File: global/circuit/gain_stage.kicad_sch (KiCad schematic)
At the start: 9 parts, among them U3 TL081H

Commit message: distortion rev 3
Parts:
- Gain1: footprint Connector_PinHeader_2.54mm:PinHeader_1x03_P2.54mm_Vertical -> effect_pedal:potentiometer_wired_23_connected
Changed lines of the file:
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@@
       (effects (font (size 1.27 1.27)) hide)
     )
-    (property "Footprint" "Connector_PinHeader_2.54mm:PinHeader_1x03_P2.54mm_Vertical" (id 2) (at 111.76 64.77 0)
+    (property "Footprint" "effect_pedal:potentiometer_wired_23_connected" (id 2) (at 111.76 64.77 0)
       (effects (font (size 1.27 1.27)) hide)
     )

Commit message: rework global circuits
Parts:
- renumbered C6 to C?, C8 to C?, C7 to C?, Gain1 to Gain?, R5 to R?, R2 to R?, R4 to R?, TP6 to TP?, U3 to U?
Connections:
- net effect_out renamed gain_in
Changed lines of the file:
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@@
     )
   )
-  (global_label "effect_out" (shape input) (at 66.04 56.515 180) (fields_autoplaced)
+  (global_label "gain_in" (shape input) (at 66.04 56.515 180) (fields_autoplaced)
     (effects (font (size 1.27 1.27)) (justify right))
-    (property "Intersheet References" "${INTERSHEET_REFS}" (id 0) (at 54.1926 56.4356 0)
+    (property "Intersheet References" "${INTERSHEET_REFS}" (id 0) (at 56.8536 56.4356 0)
       (effects (font (size 1.27 1.27)) (justify right) hide)
     )
@@
   (symbol (lib_id "Device:C") (at 111.125 41.91 0) (unit 1)
     (in_bom yes) (on_board yes)
-    (property "Reference" "C6" (id 0) (at 112.395 40.005 0)
+    (property "Reference" "C?" (id 0) (at 112.395 40.005 0)
       (effects (font (size 1.27 1.27)) (justify left))
     )
@@
   (symbol (lib_id "Device:R") (at 122.555 64.77 270) (unit 1)
     (in_bom yes) (on_board yes)
-    (property "Reference" "R5" (id 0) (at 122.555 69.85 90))
+    (property "Reference" "R?" (id 0) (at 122.555 69.85 90))
     (property "Value" "R" (id 1) (at 122.555 67.31 90)
       (effects (font (size 1.27 1.27)) hide)
@@
   (symbol (lib_id "Device:R_Potentiometer") (at 111.76 64.77 270) (unit 1)
     (in_bom yes) (on_board yes)
-    (property "Reference" "Gain1" (id 0) (at 111.76 69.85 90))
+    (property "Reference" "Gain?" (id 0) (at 111.76 69.85 90))
     (property "Value" "10k" (id 1) (at 111.76 71.12 90)
       (effects (font (size 1.27 1.27)) hide)
@@
   (symbol (lib_id "Amplifier_Operational:TL081H") (at 101.6 53.975 0) (unit 1)
     (in_bom yes) (on_board yes)
-    (property "Reference" "U3" (id 0) (at 106.045 59.055 0))
+    (property "Reference" "U?" (id 0) (at 106.045 59.055 0))
     (property "Value" "TL081H" (id 1) (at 108.585 57.15 0))
     (property "Footprint" "Package_TO_SOT_SMD:SOT-23-5_HandSoldering" (id 2) (at 101.6 53.975 0)
@@
   (symbol (lib_id "Device:R") (at 74.295 56.515 270) (unit 1)
     (in_bom yes) (on_board yes)
-    (property "Reference" "R2" (id 0) (at 74.295 53.975 90))
+    (property "Reference" "R?" (id 0) (at 74.295 53.975 90))
     (property "Value" "R" (id 1) (at 74.295 52.07 90)
       (effects (font (size 1.27 1.27)) hide)
@@
   (symbol (lib_id "power:GND") (at 101.6 73.66 0) (unit 1)
     (in_bom yes) (on_board yes) (fields_autoplaced)
-    (property "Reference" "#PWR0104" (id 0) (at 101.6 80.01 0)
+    (property "Reference" "#PWR?" (id 0) (at 101.6 80.01 0)
       (effects (font (size 1.27 1.27)) hide)
     )
@@
   (symbol (lib_id "Device:C") (at 134.62 53.975 90) (unit 1)
     (in_bom yes) (on_board yes)
-    (property "Reference" "C8" (id 0) (at 134.62 58.42 90))
+    (property "Reference" "C?" (id 0) (at 134.62 58.42 90))
     (property "Value" "C" (id 1) (at 134.62 57.785 90)
       (effects (font (size 1.27 1.27)) hide)
@@
   (symbol (lib_id "power:GND") (at 111.125 45.72 0) (unit 1)
     (in_bom yes) (on_board yes)
-    (property "Reference" "#PWR0102" (id 0) (at 111.125 52.07 0)
+    (property "Reference" "#PWR?" (id 0) (at 111.125 52.07 0)
       (effects (font (size 1.27 1.27)) hide)
     )
@@
   (symbol (lib_id "power:+4V") (at 84.455 73.66 180) (unit 1)
     (in_bom yes) (on_board yes) (fields_autoplaced)
-    (property "Reference" "#PWR0115" (id 0) (at 84.455 69.85 0)
+    (property "Reference" "#PWR?" (id 0) (at 84.455 69.85 0)
       (effects (font (size 1.27 1.27)) hide)
     )
@@
   (symbol (lib_id "power:+8V") (at 101.6 37.465 0) (unit 1)
     (in_bom yes) (on_board yes)
-    (property "Reference" "#PWR024" (id 0) (at 101.6 41.275 0)
+    (property "Reference" "#PWR?" (id 0) (at 101.6 41.275 0)
       (effects (font (size 1.27 1.27)) hide)
     )
@@
   (symbol (lib_id "Connector:TestPoint") (at 128.905 53.975 0) (unit 1)
     (in_bom yes) (on_board yes)
-    (property "Reference" "TP6" (id 0) (at 127 48.26 0)
+    (property "Reference" "TP?" (id 0) (at 127 48.26 0)
       (effects (font (size 1.27 1.27)) (justify left))
     )
@@
   (symbol (lib_id "Device:R") (at 84.455 65.405 0) (unit 1)
     (in_bom yes) (on_board yes)
-    (property "Reference" "R4" (id 0) (at 86.36 65.405 0)
+    (property "Reference" "R?" (id 0) (at 86.36 65.405 0)
       (effects (font (size 1.27 1.27)) (justify left))
     )
@@
   (symbol (lib_id "Device:C") (at 120.65 41.91 0) (unit 1)
     (in_bom yes) (on_board yes)
-    (property "Reference" "C7" (id 0) (at 121.92 40.005 0)
+    (property "Reference" "C?" (id 0) (at 121.92 40.005 0)
       (effects (font (size 1.27 1.27)) (justify left))
     )
@@
   (symbol (lib_id "power:GND") (at 120.65 45.72 0) (unit 1)
     (in_bom yes) (on_board yes)
-    (property "Reference" "#PWR0103" (id 0) (at 120.65 52.07 0)
-      (effects (font (size 1.27 1.27)) hide)
-    )
+    (property "Reference" "#PWR?" (id 0) (at 120.65 52.07 0)
+      (effects (font (size 1.27 1.27)) hide)
+    )

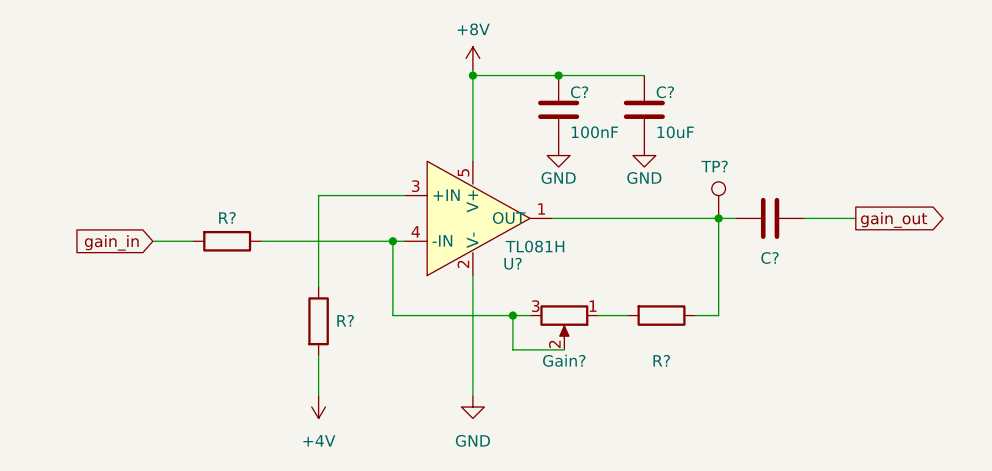
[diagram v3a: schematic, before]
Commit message: minor circuit rework for better use with multiple projects
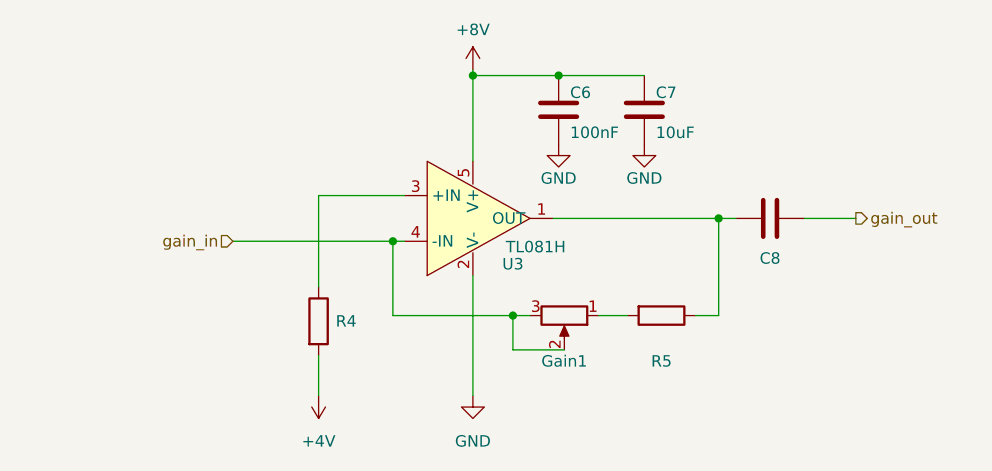
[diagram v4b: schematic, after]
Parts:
- removed R?: R, Resistor_SMD:R_0805_2012Metric_Pad1.20x1.40mm_HandSolder, symbol Device:R
- removed TP?: TestPoint, TestPoint:TestPoint_THTPad_1.0x1.0mm_Drill0.5mm, symbol Connector:TestPoint
- gave numbers to parts that had none: 7
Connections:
- net gain_in: now also Gain1.2, Gain1.3, U3.4 (-IN)
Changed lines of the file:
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@@
-    (stroke (width 0) (type default) (color 0 0 0 0))
-  )
-  (wire (pts (xy 66.04 56.515) (xy 70.485 56.515))
     (stroke (width 0) (type default) (color 0 0 0 0))
   )
@@
     (stroke (width 0) (type default) (color 0 0 0 0))
   )
-  (wire (pts (xy 78.105 56.515) (xy 92.71 56.515))
+  (wire (pts (xy 74.93 56.515) (xy 92.71 56.515))
     (stroke (width 0) (type default) (color 0 0 0 0))
   )
@@
     (stroke (width 0) (type default) (color 0 0 0 0))
   )
-  (global_label "gain_out" (shape output) (at 144.145 53.975 0) (fields_autoplaced)
+  (hierarchical_label "gain_in" (shape input) (at 74.93 56.515 180)
+    (effects (font (size 1.27 1.27)) (justify right))
+  )
+  (hierarchical_label "gain_out" (shape output) (at 144.145 53.975 0)
     (effects (font (size 1.27 1.27)) (justify left))
-    (property "Intersheet References" "${INTERSHEET_REFS}" (id 0) (at 154.6014 53.8956 0)
-      (effects (font (size 1.27 1.27)) (justify left) hide)
-    )
-  )
-  (global_label "gain_in" (shape input) (at 66.04 56.515 180) (fields_autoplaced)
-    (effects (font (size 1.27 1.27)) (justify right))
-    (property "Intersheet References" "${INTERSHEET_REFS}" (id 0) (at 56.8536 56.4356 0)
-      (effects (font (size 1.27 1.27)) (justify right) hide)
-    )
   )
   (symbol (lib_id "Device:C") (at 111.125 41.91 0) (unit 1)
     (in_bom yes) (on_board yes)
-    (property "Reference" "C?" (id 0) (at 112.395 40.005 0)
+    (property "Reference" "C6" (id 0) (at 112.395 40.005 0)
       (effects (font (size 1.27 1.27)) (justify left))
     )
@@
   (symbol (lib_id "Device:R") (at 122.555 64.77 270) (unit 1)
     (in_bom yes) (on_board yes)
-    (property "Reference" "R?" (id 0) (at 122.555 69.85 90))
+    (property "Reference" "R5" (id 0) (at 122.555 69.85 90))
     (property "Value" "R" (id 1) (at 122.555 67.31 90)
       (effects (font (size 1.27 1.27)) hide)
@@
   (symbol (lib_id "Device:R_Potentiometer") (at 111.76 64.77 270) (unit 1)
     (in_bom yes) (on_board yes)
-    (property "Reference" "Gain?" (id 0) (at 111.76 69.85 90))
+    (property "Reference" "Gain1" (id 0) (at 111.76 69.85 90))
     (property "Value" "10k" (id 1) (at 111.76 71.12 90)
       (effects (font (size 1.27 1.27)) hide)
@@
   (symbol (lib_id "Amplifier_Operational:TL081H") (at 101.6 53.975 0) (unit 1)
     (in_bom yes) (on_board yes)
-    (property "Reference" "U?" (id 0) (at 106.045 59.055 0))
+    (property "Reference" "U3" (id 0) (at 106.045 59.055 0))
     (property "Value" "TL081H" (id 1) (at 108.585 57.15 0))
     (property "Footprint" "Package_TO_SOT_SMD:SOT-23-5_HandSoldering" (id 2) (at 101.6 53.975 0)
@@
     (pin "5")
   )
-  (symbol (lib_id "Device:R") (at 74.295 56.515 270) (unit 1)
-    (in_bom yes) (on_board yes)
-    (property "Reference" "R?" (id 0) (at 74.295 53.975 90))
-    (property "Value" "R" (id 1) (at 74.295 52.07 90)
-      (effects (font (size 1.27 1.27)) hide)
-    )
-    (property "Footprint" "Resistor_SMD:R_0805_2012Metric_Pad1.20x1.40mm_HandSolder" (id 2) (at 74.295 54.737 90)
-      (effects (font (size 1.27 1.27)) hide)
-    )
-    (property "Datasheet" "~" (id 3) (at 74.295 56.515 0)
-      (effects (font (size 1.27 1.27)) hide)
-    )
-    (pin "1")
-    (pin "2")
-  )
   (symbol (lib_id "power:GND") (at 101.6 73.66 0) (unit 1)
     (in_bom yes) (on_board yes) (fields_autoplaced)
-    (property "Reference" "#PWR?" (id 0) (at 101.6 80.01 0)
+    (property "Reference" "#PWR0104" (id 0) (at 101.6 80.01 0)
       (effects (font (size 1.27 1.27)) hide)
     )
@@
   (symbol (lib_id "Device:C") (at 134.62 53.975 90) (unit 1)
     (in_bom yes) (on_board yes)
-    (property "Reference" "C?" (id 0) (at 134.62 58.42 90))
+    (property "Reference" "C8" (id 0) (at 134.62 58.42 90))
     (property "Value" "C" (id 1) (at 134.62 57.785 90)
       (effects (font (size 1.27 1.27)) hide)
@@
   (symbol (lib_id "power:GND") (at 111.125 45.72 0) (unit 1)
     (in_bom yes) (on_board yes)
-    (property "Reference" "#PWR?" (id 0) (at 111.125 52.07 0)
+    (property "Reference" "#PWR0102" (id 0) (at 111.125 52.07 0)
       (effects (font (size 1.27 1.27)) hide)
     )
@@
   (symbol (lib_id "power:+4V") (at 84.455 73.66 180) (unit 1)
     (in_bom yes) (on_board yes) (fields_autoplaced)
-    (property "Reference" "#PWR?" (id 0) (at 84.455 69.85 0)
+    (property "Reference" "#PWR0115" (id 0) (at 84.455 69.85 0)
       (effects (font (size 1.27 1.27)) hide)
     )
@@
   (symbol (lib_id "power:+8V") (at 101.6 37.465 0) (unit 1)
     (in_bom yes) (on_board yes)
-    (property "Reference" "#PWR?" (id 0) (at 101.6 41.275 0)
+    (property "Reference" "#PWR024" (id 0) (at 101.6 41.275 0)
       (effects (font (size 1.27 1.27)) hide)
     )
@@
     (pin "1")
   )
-  (symbol (lib_id "Connector:TestPoint") (at 128.905 53.975 0) (unit 1)
-    (in_bom yes) (on_board yes)
-    (property "Reference" "TP?" (id 0) (at 127 48.26 0)
-      (effects (font (size 1.27 1.27)) (justify left))
-    )
-    (property "Value" "TestPoint" (id 1) (at 131.445 51.9429 0)
-      (effects (font (size 1.27 1.27)) (justify left) hide)
-    )
-    (property "Footprint" "TestPoint:TestPoint_THTPad_1.0x1.0mm_Drill0.5mm" (id 2) (at 133.985 53.975 0)
-      (effects (font (size 1.27 1.27)) hide)
-    )
-    (property "Datasheet" "~" (id 3) (at 133.985 53.975 0)
-      (effects (font (size 1.27 1.27)) hide)
-    )
-    (pin "1")
-  )
   (symbol (lib_id "Device:R") (at 84.455 65.405 0) (unit 1)
     (in_bom yes) (on_board yes)
-    (property "Reference" "R?" (id 0) (at 86.36 65.405 0)
+    (property "Reference" "R4" (id 0) (at 86.36 65.405 0)
       (effects (font (size 1.27 1.27)) (justify left))
     )
@@
   (symbol (lib_id "Device:C") (at 120.65 41.91 0) (unit 1)
     (in_bom yes) (on_board yes)
-    (property "Reference" "C?" (id 0) (at 121.92 40.005 0)
+    (property "Reference" "C7" (id 0) (at 121.92 40.005 0)
       (effects (font (size 1.27 1.27)) (justify left))
     )
@@
   (symbol (lib_id "power:GND") (at 120.65 45.72 0) (unit 1)
     (in_bom yes) (on_board yes)
-    (property "Reference" "#PWR?" (id 0) (at 120.65 52.07 0)
-      (effects (font (size 1.27 1.27)) hide)
-    )
+    (property "Reference" "#PWR0103" (id 0) (at 120.65 52.07 0)
+      (effects (font (size 1.27 1.27)) hide)
+    )
